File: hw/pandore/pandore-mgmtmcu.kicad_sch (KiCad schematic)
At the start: 21 parts, among them J17 GROVE, J18 GROVE, J25 DISPLAY, Q10 MOSFET_EN-N, Q8 MOSFET_EN-N, Q9 MOSFET_EN-N

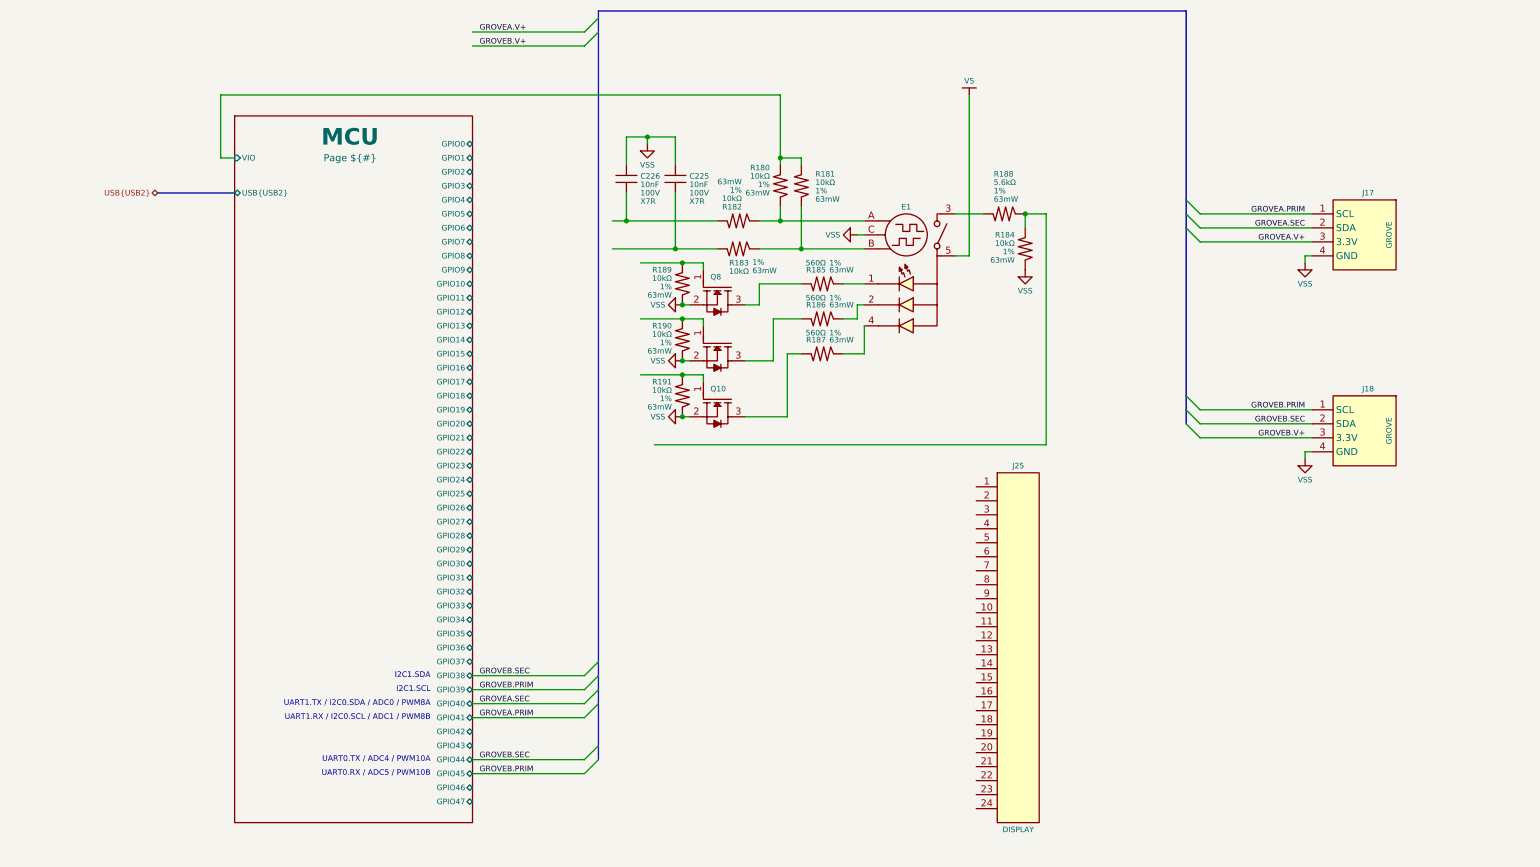
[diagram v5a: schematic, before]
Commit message: lcd control circuit added fan interface added rgba output pinout for management mcu accessories done
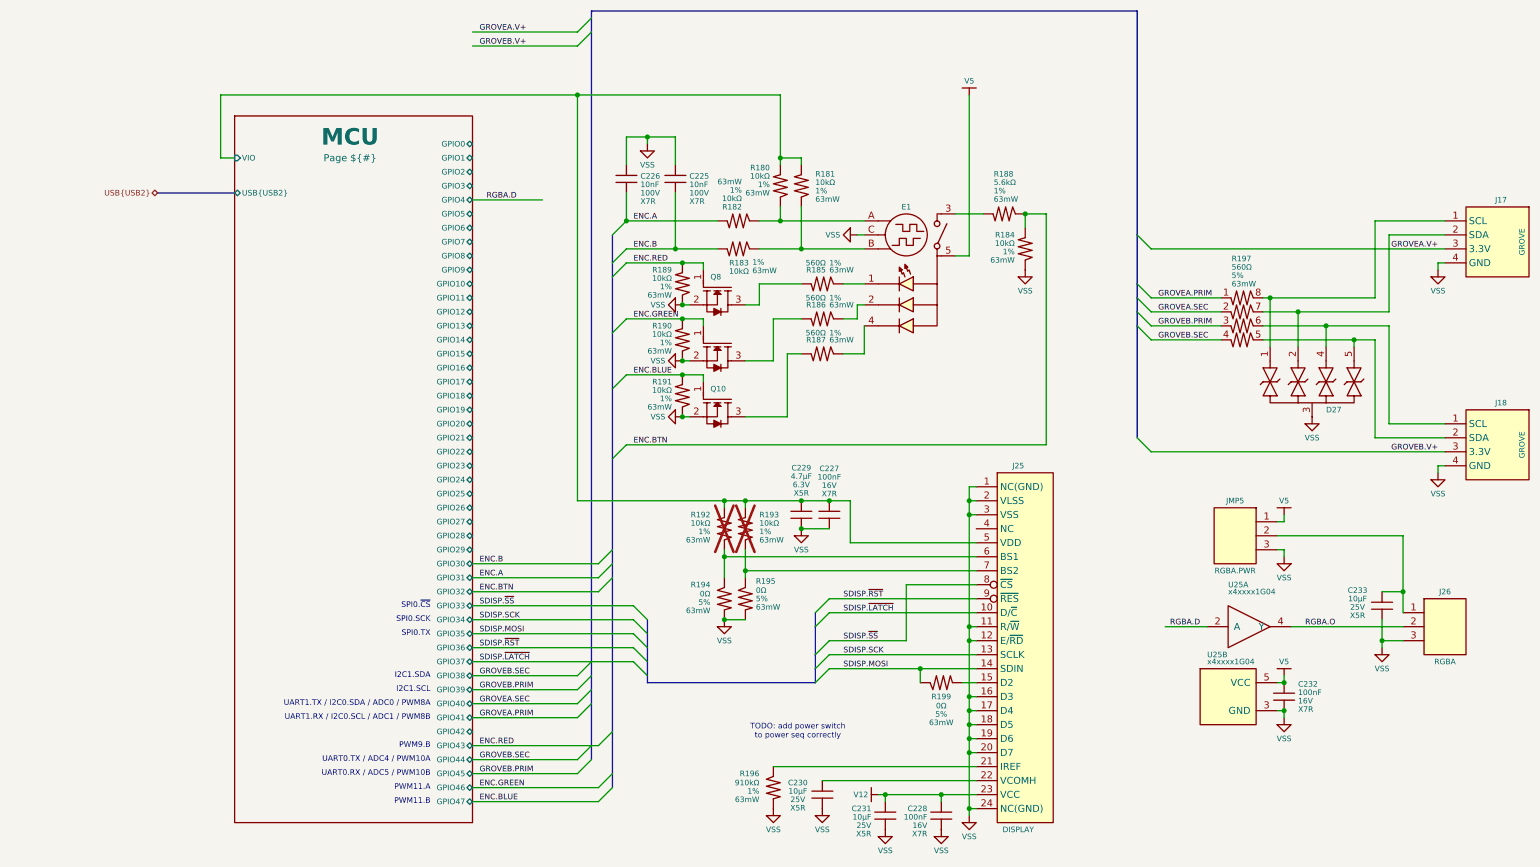
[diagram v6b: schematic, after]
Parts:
- added C227, C228, C229, C232: ${Capacitance}, ${Voltage}, ${Dielectric}, reekilib_cap:CAPC1005, symbol reekilib_cap:cap
- added C230, C231, C233: ${Capacitance}, ${Voltage}, ${Dielectric}, reekilib_cap:CAPC2012, symbol reekilib_cap:cap
- added D27: ${Vbr}, reekilib_dfn:DFN50P100X250X55-10_ESD204, symbol reekilib_tvs:diode_tvsbi_4
- added J26: RGBA, reekilib_con:HDR254P1X03-TH, symbol reekilib_con:hdr-1x3
- added JMP5: RGBA.PWR, reekilib_con:HDR254P1X03-TH, symbol reekilib_con:hdr-1x3
- added R192, R193, R194, R195, R196, R199: ${Resistance}, ${Tolerance}, ${Power}, reekilib_res:RESC1005, symbol reekilib_res:res
- added R197: ${Resistance}, ${Tolerance}, ${Power}, reekilib_res:RESCAXSR50P200X100X35-8, symbol reekilib_res:res_4
- added U25: x4xxxx1G04, reekilib_sot:SOT65P210X90-5, symbol reekilib_log:x4xxxx1G04
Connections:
- net GROVEA.PRIM: now also R197.1; no longer J17.1 (D0)
- net GROVEA.SEC: now also R197.2; no longer J17.2 (D1)
- net GROVEB.PRIM: now also R197.3; no longer J18.1 (D0)
- net GROVEB.SEC: now also R197.4; no longer J18.2 (D1)
- net MCU/VIO: now also J25.5 (VDD), C227.2, C229.2, R192.1, R193.1
- net V5: now also C232.2, JMP5.1, U25.5 (VCC)
- net VSS: now also J25.1 (NC(GND)), J25.11 (R/~{W}), J25.12 (E/~{RD}), J25.16 (D3), J25.17 (D4), J25.18 (D5), J25.19 (D6), J25.2 (VLSS), J25.20 (D7), J25.24 (NC(GND)), J25.3 (VSS), C227.1, C228.1, C229.1, C230.1, C231.1, C232.1, C233.1, D27.3, J26.3, JMP5.3, R194.1, R195.1, R196.1, U25.3 (GND)
- net SDISP.~{LATCH}: now reaches J25.10 (D/~{C})
- net SDISP.SCK: now reaches J25.13 (D0)
- net SDISP.MOSI: now reaches J25.14 (D1)
- net SDISP.MOSI: now also R199.2
- net at J25.15 (D2): now also R199.1
- net at J25.21 (IREF): now also R196.2
- net at J25.22 (VCOMH): now also C230.2
- net V12: now reaches J25.23 (VCC)
- net V12: now also C228.2, C231.2
- net at J25.6 (BS1): now also R192.2, R194.2
- net at J25.7 (BS2): now also R193.2, R195.2
- net SDISP.~{SS}: now reaches J25.8 (~{CS})
- net SDISP.~{RST}: now reaches J25.9 (~{RES})
- net ENC.GREEN: now reaches Q9.1 (G), R190.1
- net ENC.RED: now reaches Q8.1 (G), R189.1
- net ENC.A: now reaches C226.1, R182.1
- net ENC.B: now reaches C225.1, R183.1
- net ENC.BLUE: now reaches Q10.1 (G), R191.1
- net ENC.BTN: now reaches R184.1, R188.2
- new net: C233.2, J26.1, JMP5.2
- new net: D27.1, J17.1 (D0), R197.8
- new net: D27.2, J17.2 (D1), R197.7
- new net: D27.4, J18.1 (D0), R197.6
- new net: D27.5, J18.2 (D1), R197.5
- new net RGBA.D: U25.2 (A)
- new net RGBA.O: J26.2, U25.4 (Y)
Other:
- note added: "PWM11.A"
- note added: "PWM11.B"
- note added: "PWM9.B"
- note added: "SPI0.SCK"
- note added: "SPI0.TX"
- note added: "SPI0.~{CS}"
- note added: "TODO: add power switch to power seq correctly"
- moved on the sheet: J17, J18

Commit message: added todos following review
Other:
- note added: "TODO: Grove power: 3.3V"
- note added: "TODO: connect to I2C pins too"
- note added: "TODO: load switch"
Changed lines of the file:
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@@
 		(company "${corp}")
+	)
+	(text "TODO: Grove power: 3.3V"
+		(exclude_from_sim no)
+		(at 234.95 66.294 0)
+		(effects
+			(font
+				(size 1.016 1.016)
+			)
+		)
 	)
 	(text "SPI0.TX"
@@
 		)
 	)
+	(text "TODO: load switch"
+		(exclude_from_sim no)
+		(at 232.664 68.58 0)
+		(effects
+			(font
+				(size 1.016 1.016)
+			)
+		)
+	)
 	(text "PWM11.B"
 		(exclude_from_sim no)
@@
 		)
 	)
+	(text "TODO: connect to I2C pins too"
+		(exclude_from_sim no)
+		(at 146.558 155.702 0)
+		(effects
+			(font
+				(size 1.016 1.016)
+			)
+		)
+	)

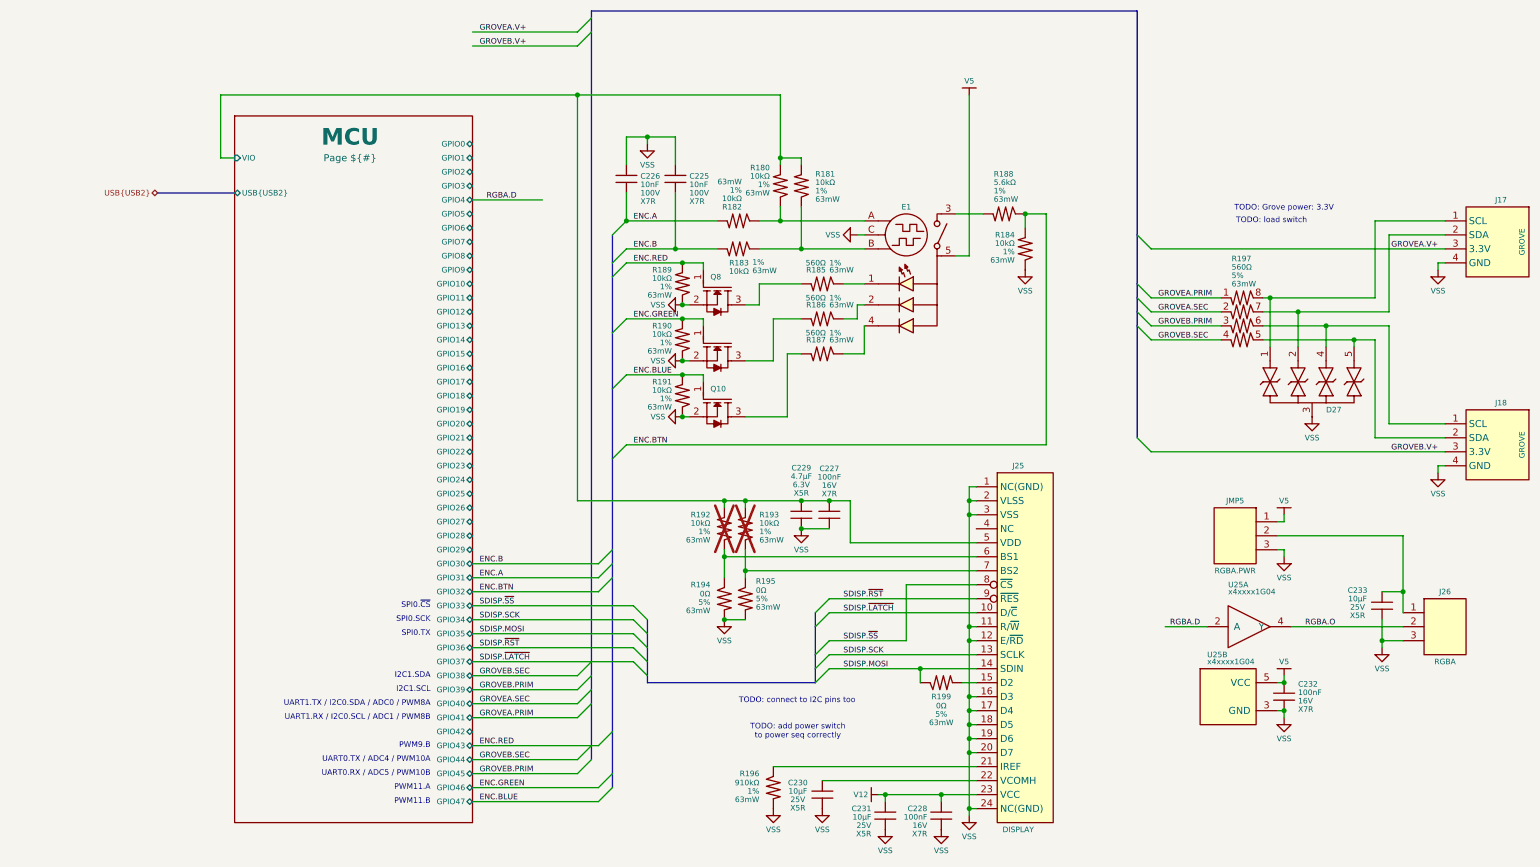
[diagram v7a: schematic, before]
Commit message: most of board control signals added, routed and defined
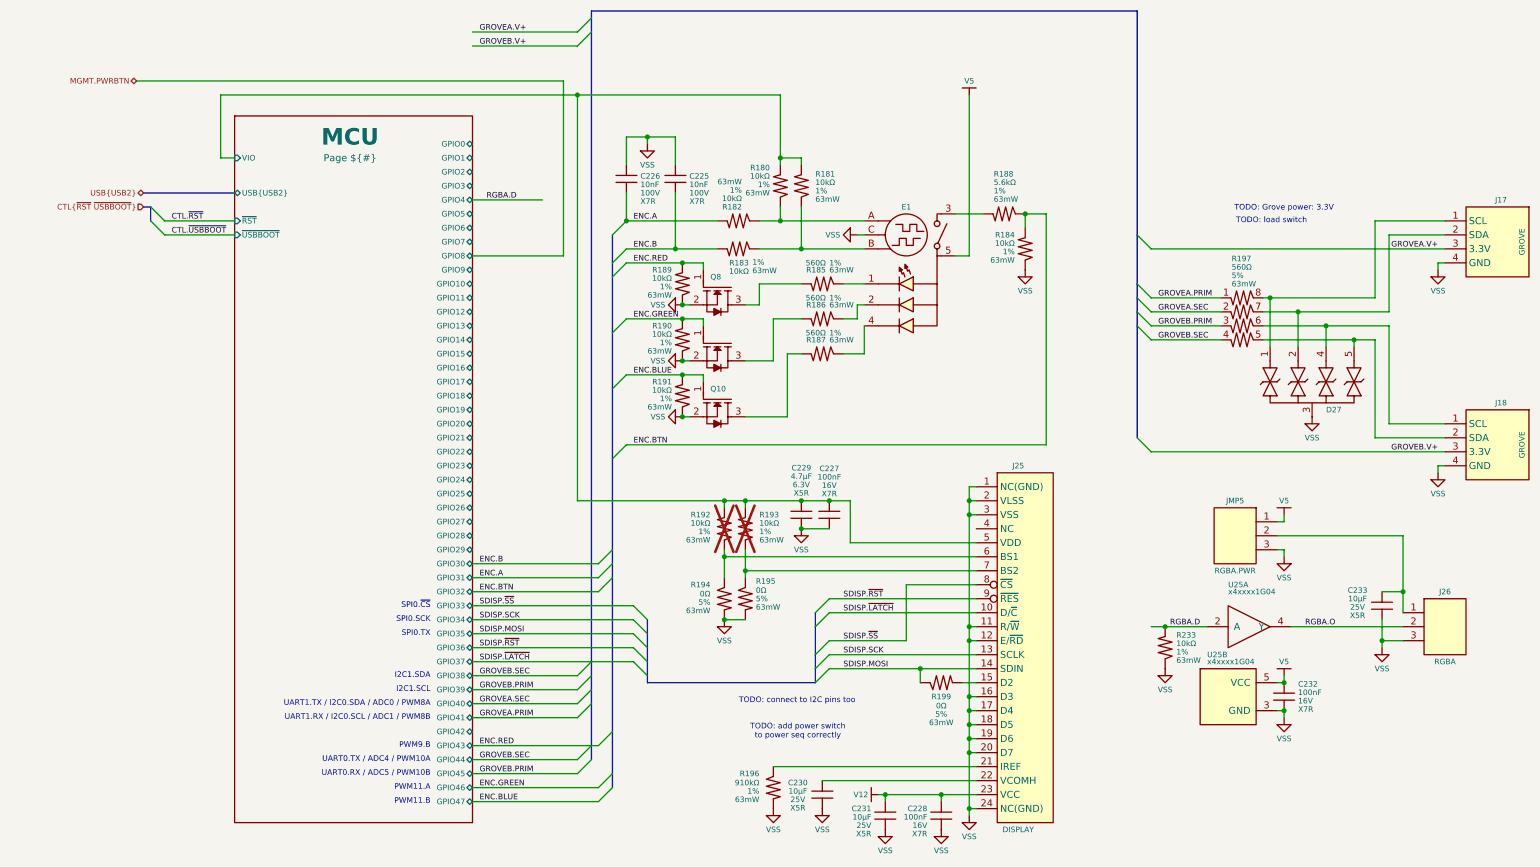
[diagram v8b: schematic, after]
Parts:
- added R233: ${Resistance}, ${Tolerance}, ${Power}, reekilib_res:RESC1005, symbol reekilib_res:res
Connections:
- net RGBA.D: now also R233.1
- net VSS: now also R233.2
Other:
- sheet MCU ports: added ~{RST}, ~{USBBOOT}; removed none
